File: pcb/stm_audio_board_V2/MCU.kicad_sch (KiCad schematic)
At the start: 9 parts, among them SW1 SW_SPST, U1 STM32H747IGTx, Y2 X1E0000210132

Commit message: pinsetup ready
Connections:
- net AD1939_I2S1_SDI: now also U1.153 (PG9); no longer U1.51 (PA6)
- net AD1939_SPI_CS: now also U1.60 (PF13)
- net POT1: now also U1.51 (PA6)
- net POT2: now also U1.52 (PA7)
- net POT3: now also U1.56 (PB1)
- net POT4: now also U1.34 (PC0)
- net POT5: now also U1.54 (PC5)
- net POT6: now also U1.58 (PF11)
- net POT_EXT: now also U1.59 (PF12)
- net SWCLK: now also U1.138 (PA14)
- net SWDIO: now also U1.132 (PA13)
- net DISPLAY_SCK: now reaches U1.1 (PE2)
- net EXT_INT_BUTTON: now reaches U1.118 (PG8)
- net TOUCH_IRQ: now reaches U1.169 (PB9)
- net DISPLAY_RST: now reaches U1.170 (PE0)
- net TOUCH_CS: now reaches U1.171 (PE1)
- net DISPLAY_CS: now reaches U1.2 (PE3)
- net DISPLAY_DC: now reaches U1.3 (PE4)
- net DISPLAY_MISO: now reaches U1.4 (PE5)
- net DISPLAY_MOSI: now reaches U1.5 (PE6)

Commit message: pcb seems to be finished drc error: 0
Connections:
- net POT1: now also U1.21 (PF3); no longer U1.51 (PA6)
- net POT2: now also U1.23 (PF5); no longer U1.52 (PA7)
- net POT3: now also U1.26 (PF6); no longer U1.56 (PB1)
- net POT4: now also U1.27 (PF7); no longer U1.34 (PC0)
- net POT5: now also U1.28 (PF8); no longer U1.54 (PC5)
- net POT6: now also U1.29 (PF9); no longer U1.58 (PF11)
- net POT_EXT: now also U1.30 (PF10); no longer U1.59 (PF12)
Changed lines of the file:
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@@
+    (stroke (width 0) (type default))
+  )
+  (wire (pts (xy 167.64 157.48) (xy 171.45 157.48))
     (stroke (width 0) (type default))
   )
@@
     (stroke (width 0) (type default))
   )
-  (wire (pts (xy 167.64 167.64) (xy 171.45 167.64))
-    (stroke (width 0) (type default))
-  )
   (wire (pts (xy 194.31 40.64) (xy 196.85 40.64))
     (stroke (width 0) (type default))
@@
     (stroke (width 0) (type default))
   )
+  (wire (pts (xy 167.64 152.4) (xy 171.45 152.4))
+    (stroke (width 0) (type default))
+  )
   (wire (pts (xy 167.64 182.88) (xy 171.45 182.88))
     (stroke (width 0) (type default))
@@
     (stroke (width 0) (type default))
   )
-  (wire (pts (xy 265.43 149.86) (xy 273.05 149.86))
-    (stroke (width 0) (type default))
-  )
-  (wire (pts (xy 265.43 68.58) (xy 275.59 68.58))
-    (stroke (width 0) (type default))
-  )
   (wire (pts (xy 209.55 43.18) (xy 209.55 40.64))
     (stroke (width 0) (type default))
@@
     (stroke (width 0) (type default))
   )
+  (wire (pts (xy 167.64 154.94) (xy 171.45 154.94))
+    (stroke (width 0) (type default))
+  )
   (wire (pts (xy 222.25 246.38) (xy 222.25 243.84))
     (stroke (width 0) (type default))
@@
     (stroke (width 0) (type default))
   )
+  (wire (pts (xy 167.64 165.1) (xy 171.45 165.1))
+    (stroke (width 0) (type default))
+  )
   (wire (pts (xy 161.29 240.03) (xy 161.29 242.57))
     (stroke (width 0) (type default))
@@
     (stroke (width 0) (type default))
   )
-  (wire (pts (xy 265.43 137.16) (xy 273.05 137.16))
-    (stroke (width 0) (type default))
-  )
   (wire (pts (xy 152.4 59.69) (xy 152.4 58.42))
     (stroke (width 0) (type default))
@@
     (stroke (width 0) (type default))
   )
-  (wire (pts (xy 265.43 96.52) (xy 275.59 96.52))
-    (stroke (width 0) (type default))
-  )
   (wire (pts (xy 219.71 246.38) (xy 219.71 243.84))
     (stroke (width 0) (type default))
@@
     (stroke (width 0) (type default))
   )
-  (wire (pts (xy 167.64 170.18) (xy 171.45 170.18))
-    (stroke (width 0) (type default))
-  )
   (wire (pts (xy 317.5 92.71) (xy 317.5 93.98))
     (stroke (width 0) (type default))
@@
     (stroke (width 0) (type default))
   )
-  (wire (pts (xy 265.43 66.04) (xy 275.59 66.04))
-    (stroke (width 0) (type default))
-  )
   (wire (pts (xy 265.43 165.1) (xy 274.32 165.1))
     (stroke (width 0) (type default))
@@
     (stroke (width 0) (type default))
   )
+  (wire (pts (xy 167.64 162.56) (xy 171.45 162.56))
+    (stroke (width 0) (type default))
+  )
   (wire (pts (xy 317.5 83.82) (xy 323.85 83.82))
     (stroke (width 0) (type default))
@@
     (stroke (width 0) (type default))
   )
+  (wire (pts (xy 167.64 147.32) (xy 171.45 147.32))
+    (stroke (width 0) (type default))
+  )
   (wire (pts (xy 330.2 35.56) (xy 330.2 33.02))
+    (stroke (width 0) (type default))
+  )
+  (wire (pts (xy 167.64 160.02) (xy 171.45 160.02))
     (stroke (width 0) (type default))
   )
@@
     )
   )
-  (global_label "POT5" (shape input) (at 273.05 149.86 0) (fields_autoplaced)
-    (effects (font (size 1.27 1.27)) (justify left))
-    (property "Intersheetrefs" "${INTERSHEET_REFS}" (at 280.7334 149.86 0)
-      (effects (font (size 1.27 1.27)) (justify left) hide)
+  (global_label "POT5" (shape input) (at 167.64 160.02 180) (fields_autoplaced)
+    (effects (font (size 1.27 1.27)) (justify right))
+    (property "Intersheetrefs" "${INTERSHEET_REFS}" (at 159.9566 160.02 0)
+      (effects (font (size 1.27 1.27)) (justify right) hide)
     )
   )
@@
     )
   )
-  (global_label "POT1" (shape input) (at 275.59 66.04 0) (fields_autoplaced)
-    (effects (font (size 1.27 1.27)) (justify left))
-    (property "Intersheetrefs" "${INTERSHEET_REFS}" (at 283.2734 66.04 0)
-      (effects (font (size 1.27 1.27)) (justify left) hide)
+  (global_label "POT1" (shape input) (at 167.64 147.32 180) (fields_autoplaced)
+    (effects (font (size 1.27 1.27)) (justify right))
+    (property "Intersheetrefs" "${INTERSHEET_REFS}" (at 159.9566 147.32 0)
+      (effects (font (size 1.27 1.27)) (justify right) hide)
     )
   )
@@
     )
   )
-  (global_label "POT4" (shape input) (at 273.05 137.16 0) (fields_autoplaced)
-    (effects (font (size 1.27 1.27)) (justify left))
-    (property "Intersheetrefs" "${INTERSHEET_REFS}" (at 280.7334 137.16 0)
-      (effects (font (size 1.27 1.27)) (justify left) hide)
+  (global_label "POT4" (shape input) (at 167.64 157.48 180) (fields_autoplaced)
+    (effects (font (size 1.27 1.27)) (justify right))
+    (property "Intersheetrefs" "${INTERSHEET_REFS}" (at 159.9566 157.48 0)
+      (effects (font (size 1.27 1.27)) (justify right) hide)
     )
   )
@@
     )
   )
-  (global_label "POT_EXT" (shape input) (at 167.64 170.18 180) (fields_autoplaced)
-    (effects (font (size 1.27 1.27)) (justify right))
-    (property "Intersheetrefs" "${INTERSHEET_REFS}" (at 156.8724 170.18 0)
+  (global_label "POT_EXT" (shape input) (at 167.64 165.1 180) (fields_autoplaced)
+    (effects (font (size 1.27 1.27)) (justify right))
+    (property "Intersheetrefs" "${INTERSHEET_REFS}" (at 156.8724 165.1 0)
       (effects (font (size 1.27 1.27)) (justify right) hide)
     )
@@
     )
   )
-  (global_label "POT3" (shape input) (at 275.59 96.52 0) (fields_autoplaced)
-    (effects (font (size 1.27 1.27)) (justify left))
-    (property "Intersheetrefs" "${INTERSHEET_REFS}" (at 283.2734 96.52 0)
-      (effects (font (size 1.27 1.27)) (justify left) hide)
+  (global_label "POT3" (shape input) (at 167.64 154.94 180) (fields_autoplaced)
+    (effects (font (size 1.27 1.27)) (justify right))
+    (property "Intersheetrefs" "${INTERSHEET_REFS}" (at 159.9566 154.94 0)
+      (effects (font (size 1.27 1.27)) (justify right) hide)
     )
   )
@@
     )
   )
-  (global_label "POT6" (shape input) (at 167.64 167.64 180) (fields_autoplaced)
-    (effects (font (size 1.27 1.27)) (justify right))
-    (property "Intersheetrefs" "${INTERSHEET_REFS}" (at 159.9566 167.64 0)
+  (global_label "POT6" (shape input) (at 167.64 162.56 180) (fields_autoplaced)
+    (effects (font (size 1.27 1.27)) (justify right))
+    (property "Intersheetrefs" "${INTERSHEET_REFS}" (at 159.9566 162.56 0)
       (effects (font (size 1.27 1.27)) (justify right) hide)
     )
@@
     )
   )
-  (global_label "POT2" (shape input) (at 275.59 68.58 0) (fields_autoplaced)
-    (effects (font (size 1.27 1.27)) (justify left))
-    (property "Intersheetrefs" "${INTERSHEET_REFS}" (at 283.2734 68.58 0)
-      (effects (font (size 1.27 1.27)) (justify left) hide)
-    )
-  )
+  (global_label "POT2" (shape input) (at 167.64 152.4 180) (fields_autoplaced)
+    (effects (font (size 1.27 1.27)) (justify right))
+    (property "Intersheetrefs" "${INTERSHEET_REFS}" (at 159.9566 152.4 0)
+      (effects (font (size 1.27 1.27)) (justify right) hide)
+    )
+  )

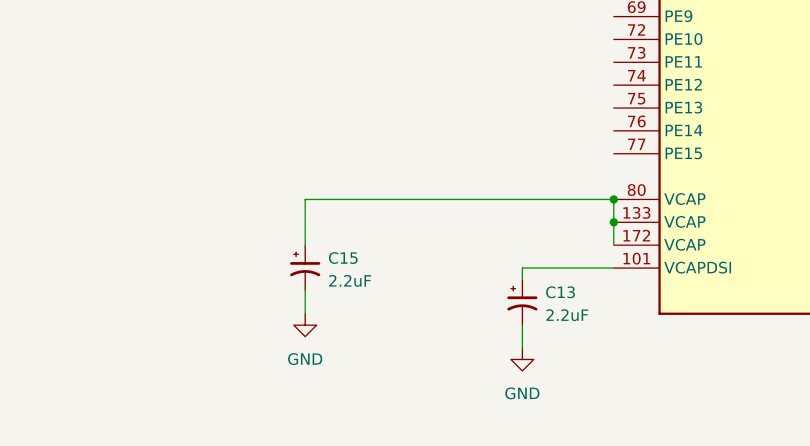
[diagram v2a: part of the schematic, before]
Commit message: silkscreen updated
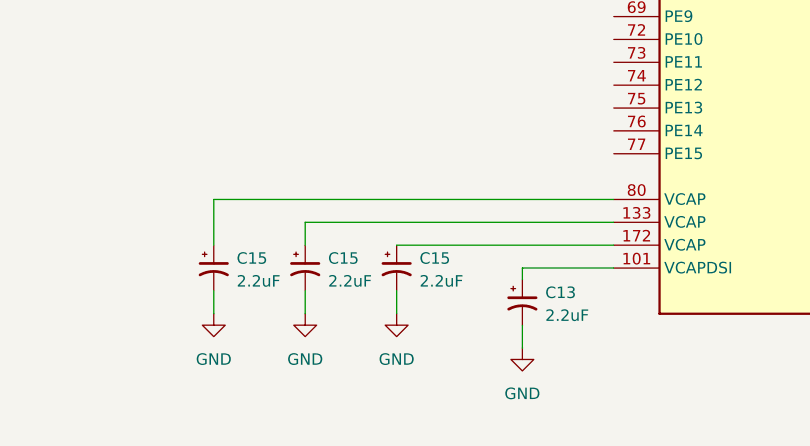
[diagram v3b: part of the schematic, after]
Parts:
- added C15 (x2): 2.2uF, Capacitor_SMD:C_0805_2012Metric_Pad1.18x1.45mm_HandSolder, symbol Device:C_Polarized_Small_US
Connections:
- net GND: now also C15.2, C15.2
- net at C15.1, U1.80 (VCAP): no longer U1.133 (VCAP), U1.172 (VCAP)
- new net: C15.1, U1.172 (VCAP)
- new net: C15.1, U1.133 (VCAP)
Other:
- moved on the sheet: C15

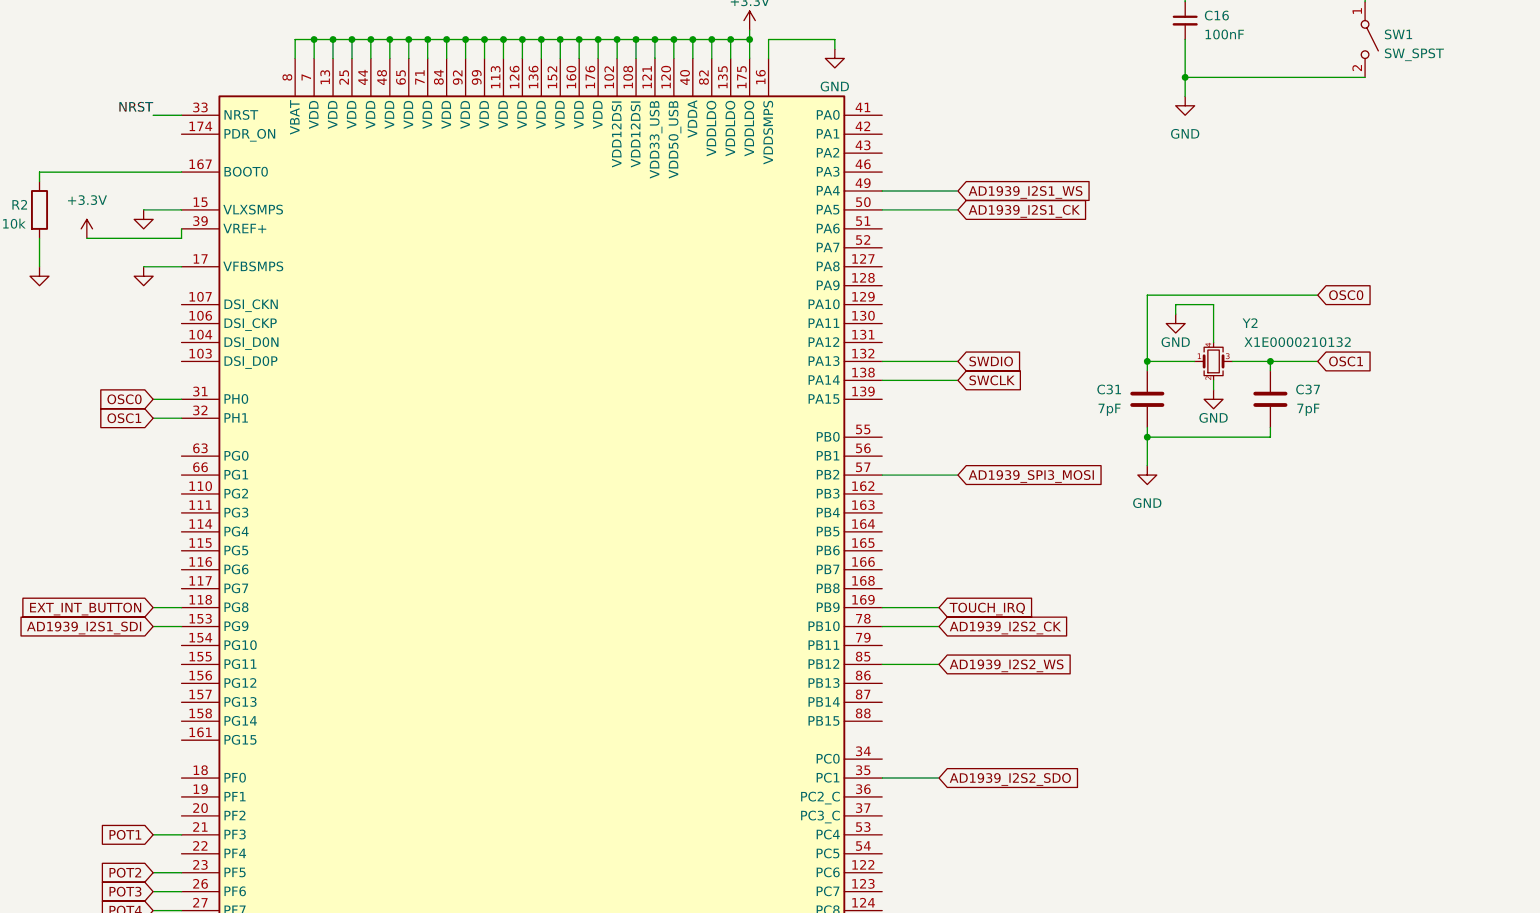
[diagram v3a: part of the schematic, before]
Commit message: stm_audio_board_V2 is finished, sent to jlcPCB for production
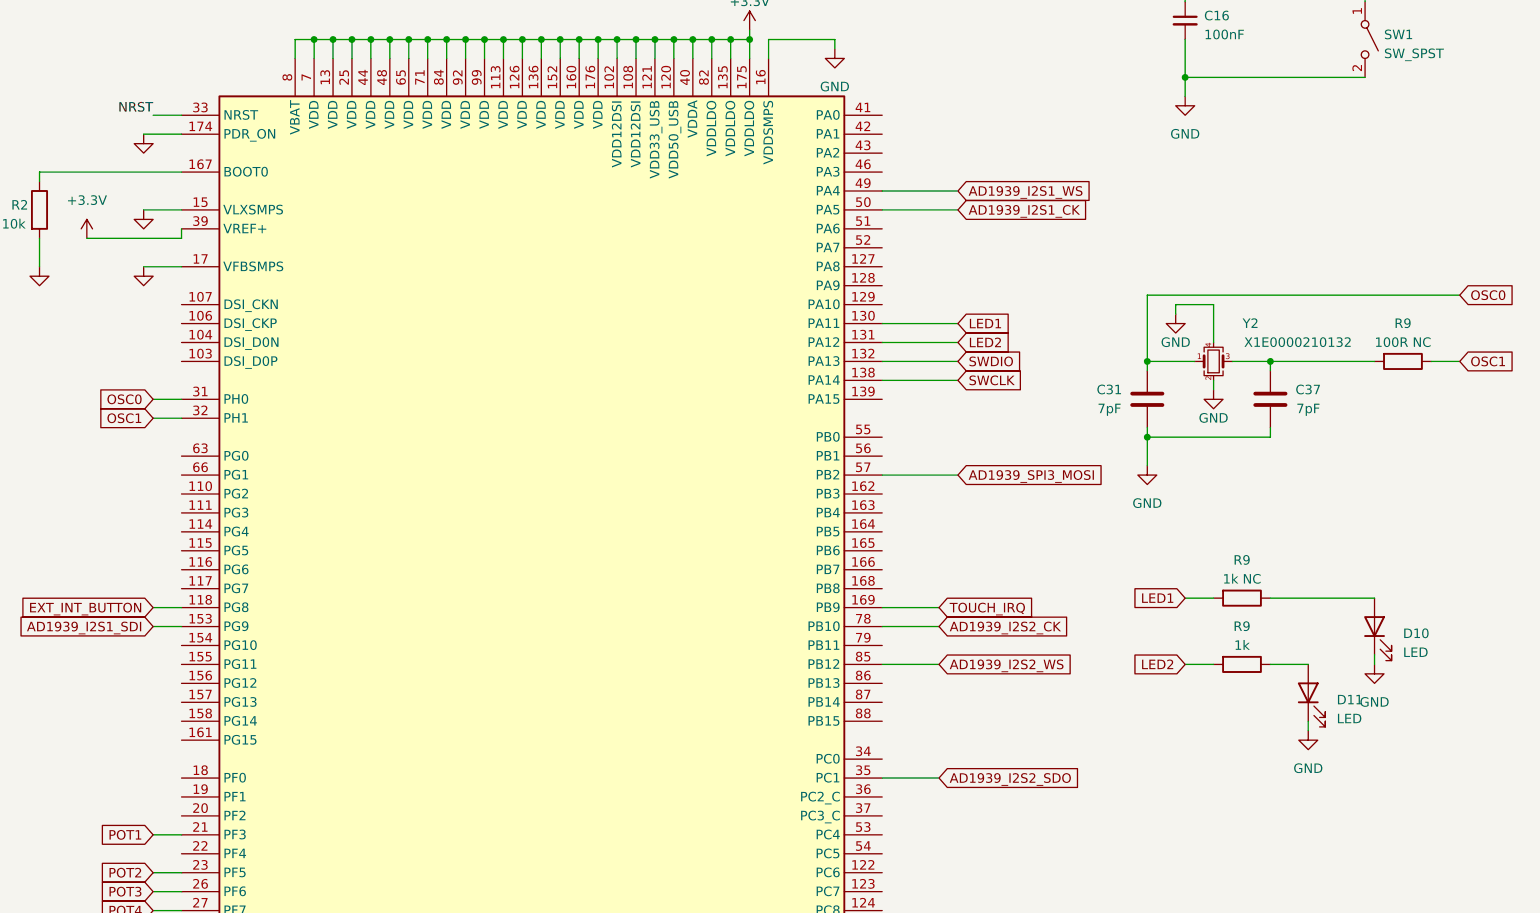
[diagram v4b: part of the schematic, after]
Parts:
- added D10, D11: LED, LED_SMD:LED_0603_1608Metric_Pad1.05x0.95mm_HandSolder, symbol Device:LED
- added R9: 1k, Resistor_SMD:R_0603_1608Metric_Pad0.98x0.95mm_HandSolder, symbol Device:R
- added R9: 100R NC, Resistor_SMD:R_0603_1608Metric_Pad0.98x0.95mm_HandSolder, symbol Device:R
- added R9: 1k NC, Resistor_SMD:R_0603_1608Metric_Pad0.98x0.95mm_HandSolder, symbol Device:R
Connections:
- net GND: now also U1.174 (PDR_ON), D10.1 (K), D11.1 (K)
- net OSC1: now also R9.1; no longer C37.2, Y2.3
- net LED1: now reaches U1.130 (PA11)
- net LED1: now also R9.2
- net LED2: now reaches U1.131 (PA12)
- net LED2: now also R9.2
- new net: D10.2 (A), R9.1
- new net: C37.2, R9.2, Y2.3
- new net: D11.2 (A), R9.1

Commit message: touchgfx fixes
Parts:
- C31, C37: value 7pF -> 9pF
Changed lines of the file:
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@@
       (effects (font (size 1.27 1.27)))
     )
-    (property "Value" "7pF" (at 295.91 90.17 0)
+    (property "Value" "9pF" (at 295.91 90.17 0)
       (effects (font (size 1.27 1.27)))
     )
@@
       (effects (font (size 1.27 1.27)))
     )
-    (property "Value" "7pF" (at 322.58 90.17 0)
-      (effects (font (size 1.27 1.27)))
-    )
+    (property "Value" "9pF" (at 322.58 90.17 0)
+      (effects (font (size 1.27 1.27)))
+    )
